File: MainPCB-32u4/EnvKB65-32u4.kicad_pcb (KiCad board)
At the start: 2 copper layers, 320.8 x 99.7 mm, 174 parts, among them U1 ATmega32U4-MU, X1 7050 8MHz 5V

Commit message: changed my mind, I wanted the 32u version to have more switches, going to figure out if I can fit the MCU somewhere on the back of the board.
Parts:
- removed the C2 at (362.3, 121.2)
- removed the C7 at (368.2, 114.6)
- removed X1: 7050 8MHz 5V, Oscillator:Oscillator_SMD_SeikoEpson_SG8002CA-4Pin_7.0x5.0mm
- added C2: 20pF 0402, Capacitor_SMD:C_0402_1005Metric, B.Cu at (329.4, 90.8)
- added C2: 15pf 0402, Capacitor_SMD:C_0402_1005Metric, B.Cu at (360.1, 78.0)
- added C7: 20pF 0402, Capacitor_SMD:C_0402_1005Metric, B.Cu at (329.4, 88.8)
- added C7: 0.1uF 0402, Capacitor_SMD:C_0402_1005Metric, B.Cu at (352.4, 74.6)
- added D_131: Diode SOD-323, Diode_SMD:D_SOD-323_HandSoldering, B.Cu at (366.5, 118.9)
- added D_132: Diode SOD-323, Diode_SMD:D_SOD-323_HandSoldering, B.Cu at (368.5, 118.9)
- added D_271: Diode SOD-323, Diode_SMD:D_SOD-323_HandSoldering, B.Cu at (366.4, 132.0)
- added D_272: Diode SOD-323, Diode_SMD:D_SOD-323_HandSoldering, B.Cu at (368.4, 132.0)
- added K_131: KEYSW, MX_Only:MXOnly-1U-NoLED, F.Cu at (358.3, 111.5)
- added K_132: KEYSW, MX_Only:MXOnly-1U-NoLED, F.Cu at (377.3, 111.5)
- added K_271: KEYSW, MX_Only:MXOnly-1U-NoLED, F.Cu at (358.3, 130.6)
- added K_272: KEYSW, MX_Only:MXOnly-1U-NoLED, F.Cu at (377.3, 130.6)
- added Y1: 8MHz 5032_2P, Crystal:Crystal_SMD_5032-2Pin_5.0x3.2mm, B.Cu at (323.9, 89.8)
- C1, C10, C11, C13, C3, C4, C5, C6, C8, R1, R3, R4, R5, R6, RSW1, U1: moved to B.Cu
- e1: footprint HRO-TYPE-C31-M-12:HRO-TYPE-C-31-M-12 -> HRO-TYPE-C31-M-12:HRO-TYPE-C-31-M-12-Assembly; moved to B.Cu
- moved C11 65.2 mm to (343.8, 72.3)
- moved C5 59.8 mm to (346.6, 72.1)
- moved C8 58.4 mm to (349.5, 74.1)
- moved C6 57.0 mm to (352.4, 72.7)
- moved R1 51.0 mm to (337.2, 71.8), turned to 0 degrees
- moved RSW1 43.3 mm to (339.1, 75.0)
- moved R5 42.4 mm to (343.8, 76.2), turned to 0 degrees
- moved R4 42.2 mm to (340.1, 71.8)
- moved C4 41.2 mm to (349.5, 72.1), turned to 0 degrees
- moved R3 39.6 mm to (343.8, 74.2)
- moved C13 37.4 mm to (351.9, 76.6), turned to 0 degrees
- moved C10 35.9 mm to (346.6, 74.1), turned to 0 degrees
- moved C1 35.3 mm to (348.4, 76.3), turned to 0 degrees
- moved C3 34.3 mm to (355.2, 76.1), turned to 0 degrees
- moved R6 31.4 mm to (357.2, 78.0), turned to 0 degrees
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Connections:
- H0 pad 1: (no net) -> GND
- H1 pad 1: (no net) -> GND
- H2 pad 1: (no net) -> GND
- H3 pad 1: (no net) -> GND
- H4 pad 1: (no net) -> GND
- H5 pad 1: (no net) -> GND
- U1 pad 1: col11 -> Net-(U1-Pad1)
- U1 pad 10: col0 -> Net-(U1-Pad10)
- U1 pad 11: col1 -> Net-(U1-Pad11)
- U1 pad 12: col2 -> Net-(U1-Pad12)
- U1 pad 18: col3 -> Net-(U1-Pad18)
- U1 pad 19: col4 -> Net-(U1-Pad19)
- U1 pad 20: col14 -> Net-(U1-Pad20)
- U1 pad 21: col15 -> Net-(U1-Pad21)
- U1 pad 22: col16 -> Net-(U1-Pad22)
- U1 pad 36: col5 -> Net-(U1-Pad36)
- U1 pad 37: col6 -> Net-(U1-Pad37)
- U1 pad 38: col7 -> Net-(U1-Pad38)
- U1 pad 39: col8 -> Net-(U1-Pad39)
- U1 pad 40: col9 -> Net-(U1-Pad40)
- U1 pad 41: col10 -> Net-(U1-Pad41)
- U1 pad 8: col12 -> Net-(U1-Pad8)
- U1 pad 9: col13 -> Net-(U1-Pad9)
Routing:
- net row2: track 351.7 -> 290.7 mm
- net VBUS: track 33.6 -> 0.00 mm, vias 9 -> 0
- net col4: track 321.8 -> 289.3 mm, vias 1 -> 0
- net col3: track 345.4 -> 313.6 mm, vias 1 -> 0
- net col15: track 45.4 -> 76.9 mm
- net GND: track 38.4 -> 8.90 mm, vias 6 -> 1
- net USB_D-: track 26.7 -> 0.00 mm, vias 4 -> 0
- net USB_D+: track 25.8 -> 0.00 mm, vias 4 -> 0
- net col16: track 52.0 -> 76.9 mm
- net col2: track 331.8 -> 307.4 mm, vias 1 -> 0
- net col0: track 397.6 -> 373.2 mm, vias 1 -> 0
- net col1: track 362.1 -> 338.5 mm, vias 1 -> 0
- net Net-(D_132-Pad2): track 0.00 -> 19.8 mm
- net col14: track 134.2 -> 116.6 mm
- net col13: track 121.1 -> 105.1 mm
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- removed copper zone on B.Cu, net VBUS

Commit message: finished running traces, probably need to clean up some bits and pieces.
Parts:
- removed the C2 at (329.4, 90.8)
- removed the C2 at (360.1, 78.0)
- removed C5, C6: 100nf 0402, Capacitor_SMD:C_0402_1005Metric
- removed the C7 at (352.4, 74.6)
- added C2: 20pF 0402, Capacitor_SMD:C_0402_1005Metric, B.Cu at (353.6, 103.7)
- added R2: 330r 0402, Resistor_SMD:R_0402_1005Metric, B.Cu at (347.0, 102.9)
- C1, C13: moved to F.Cu
- RESET: renamed from RSW1; moved to F.Cu
- moved C11 46.1 mm to (344.5, 118.4), turned to 90 degrees
- moved C13 41.6 mm to (346.7, 117.9)
- moved C3 41.5 mm to (340.7, 115.0), turned to 180 degrees
- moved C8 40.6 mm to (352.2, 114.6)
- moved R4 38.8 mm to (341.4, 110.6), turned to 315 degrees
- moved C4 37.7 mm to (342.8, 109.2), turned to 135 degrees
- moved R5 37.2 mm to (365.8, 106.3)
- moved R3 36.0 mm to (342.4, 110.2), turned to 315 degrees
- moved C10 34.4 mm to (349.4, 108.3), turned to 45 degrees
- moved C1 34.1 mm to (364.3, 106.6), turned to 180 degrees
- moved R1 33.4 mm to (345.9, 104.0), turned to 90 degrees
- moved R6 31.1 mm to (369.8, 106.4), turned to 180 degrees
- moved Y1 30.3 mm to (350.6, 104.0), turned to 135 degrees
- moved RESET 26.0 mm to (344.9, 100.3)
- moved C7 25.0 mm to (351.1, 101.2), turned to 135 degrees
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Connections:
- R1 pad 2: /RUN -> Net-(R1-Pad2)
- RESET pad 2: /RUN -> Net-(R2-Pad1)
- U1 pad 1: Net-(U1-Pad1) -> col4
- U1 pad 10: Net-(U1-Pad10) -> col1
- U1 pad 11: Net-(U1-Pad11) -> col0
- U1 pad 13: /RUN -> Net-(R1-Pad2)
- U1 pad 18: Net-(U1-Pad18) -> col15
- U1 pad 19: Net-(U1-Pad19) -> col16
- U1 pad 25: Net-(U1-Pad25) -> row4
- U1 pad 26: Net-(U1-Pad26) -> row3
- U1 pad 27: Net-(U1-Pad27) -> row2
- U1 pad 28: Net-(U1-Pad28) -> row1
- U1 pad 29: Net-(U1-Pad29) -> row0
- U1 pad 30: Net-(U1-Pad30) -> col14
- U1 pad 31: Net-(U1-Pad31) -> col5
- U1 pad 32: Net-(U1-Pad32) -> col6
- U1 pad 33: Net-(U1-Pad33) -> col7
- U1 pad 36: Net-(U1-Pad36) -> col8
- U1 pad 37: Net-(U1-Pad37) -> col9
- U1 pad 38: Net-(U1-Pad38) -> col10
- U1 pad 39: Net-(U1-Pad39) -> col11
- U1 pad 40: Net-(U1-Pad40) -> col12
- U1 pad 41: Net-(U1-Pad41) -> col13
- U1 pad 8: Net-(U1-Pad8) -> col3
- U1 pad 9: Net-(U1-Pad9) -> col2
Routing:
- net VBUS: track 0.00 -> 69.8 mm, vias 0 -> 9
- net row2: track 290.7 -> 336.1 mm, vias 0 -> 2
- net USB_D-: track 0.00 -> 38.6 mm, vias 0 -> 3
- net row4: track 327.7 -> 365.9 mm, vias 0 -> 2
- net USB_D+: track 0.00 -> 36.2 mm, vias 0 -> 3
- net col16: track 76.9 -> 105.0 mm, vias 0 -> 1
- net col5: track 245.5 -> 272.6 mm, vias 0 -> 1
- net col6: track 246.6 -> 272.5 mm, vias 0 -> 1
- net col7: track 208.1 -> 233.2 mm, vias 0 -> 1
- net col11: track 145.7 -> 168.5 mm, vias 0 -> 1
- net row1: track 280.6 -> 301.9 mm, vias 0 -> 2
- net row3: track 337.5 -> 358.3 mm, vias 0 -> 2
- net col8: track 206.0 -> 226.5 mm, vias 0 -> 1
- net col9: track 167.7 -> 187.6 mm, vias 0 -> 1
- net col10: track 169.8 -> 189.4 mm, vias 0 -> 1
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- added copper zone on F.Cu, net VBUS

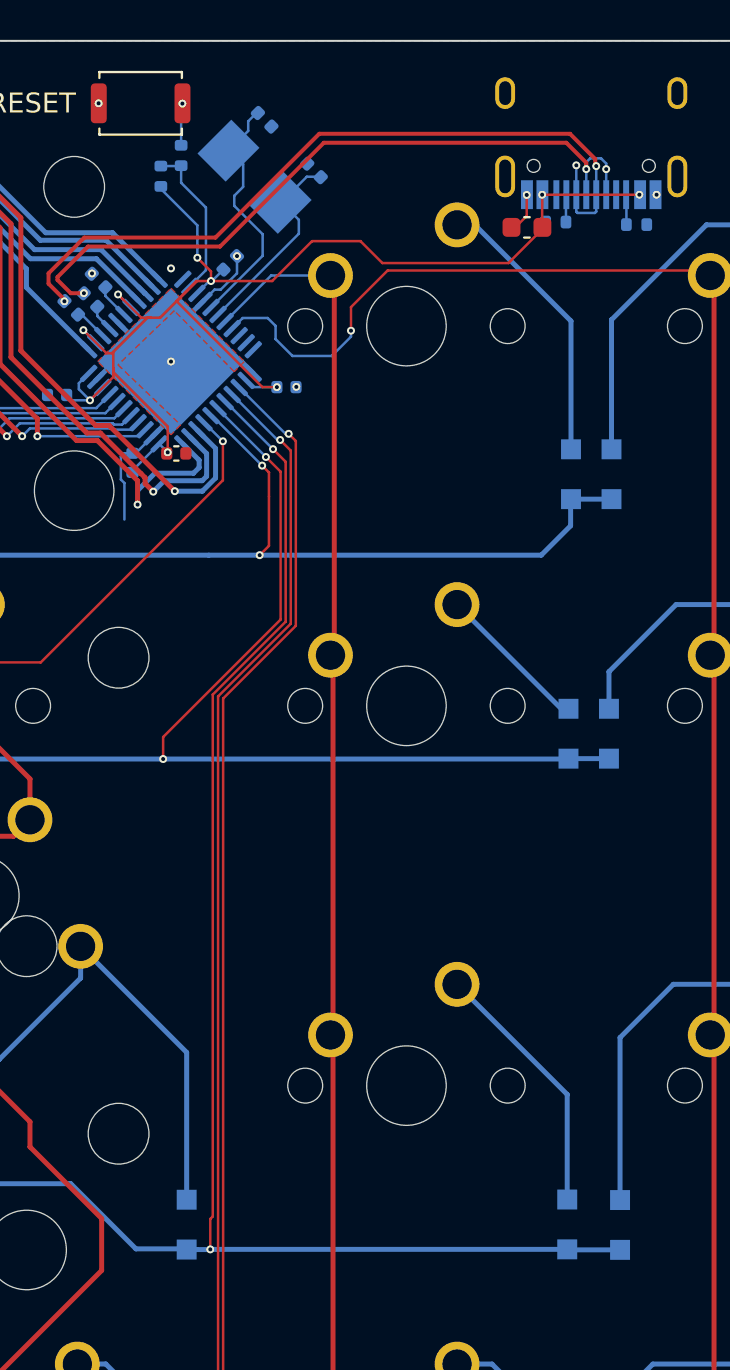
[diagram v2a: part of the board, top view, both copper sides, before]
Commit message: adjusted some bits to comply with DRC.
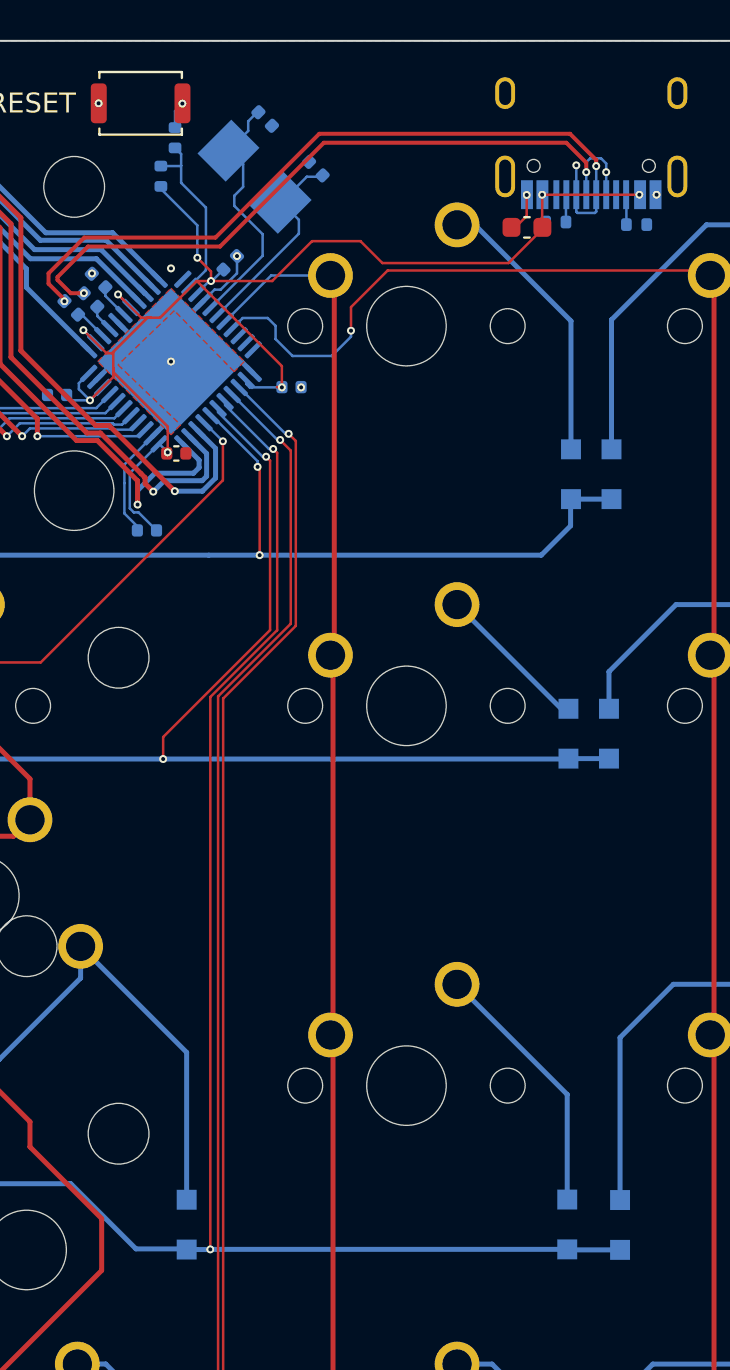
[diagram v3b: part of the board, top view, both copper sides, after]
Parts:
- moved C11 3.47 mm to (345.2, 121.8), turned to 180 degrees
- moved R2 0.94 mm to (346.7, 102.1)
- moved C8 0.25 mm to (352.5, 114.6)
- moved C2 0.13 mm to (353.7, 103.6)
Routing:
- net VBUS: track 69.8 -> 72.9 mm
- net Net-(R1-Pad2): track 7.93 -> 8.94 mm
- net Net-(R2-Pad1): track 2.14 -> 1.46 mm

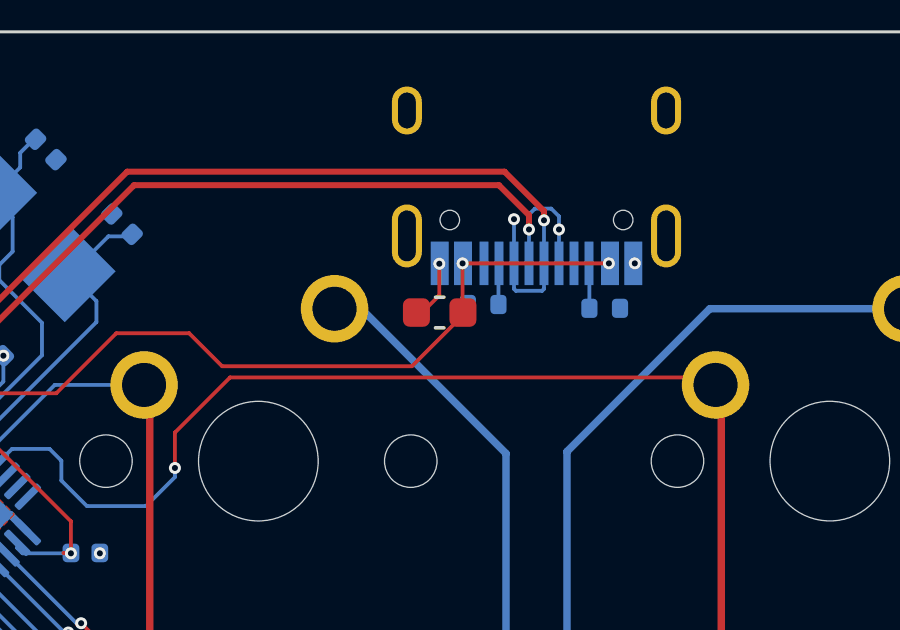
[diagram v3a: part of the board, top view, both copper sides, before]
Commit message: a decoupling capacitor was in a bad position
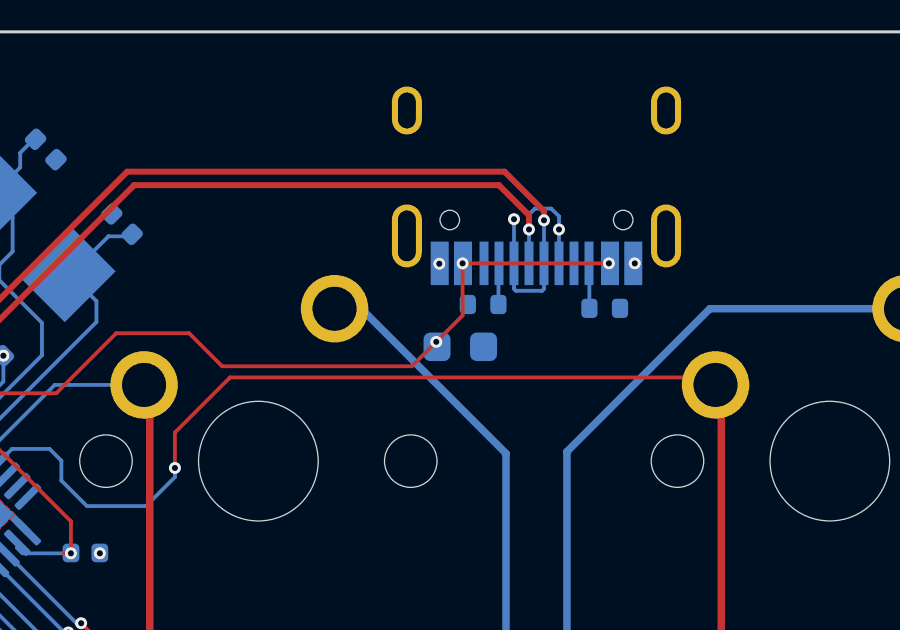
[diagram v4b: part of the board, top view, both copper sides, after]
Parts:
- C1: moved to B.Cu
- moved C1 1.33 mm to (365.0, 107.7), turned to 0 degrees
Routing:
- net GND: track 19.6 -> 17.5 mm
- net VBUS: vias 9 -> 10
